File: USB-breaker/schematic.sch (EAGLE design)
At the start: 23 parts, among them K1 G6K-2P, K3 G6K-2P, T1 BC558B, T2 BC548B, X1 PN87520-S, X2 PN87520-S, X3 10104110, X4 UX60SC-MB-5ST

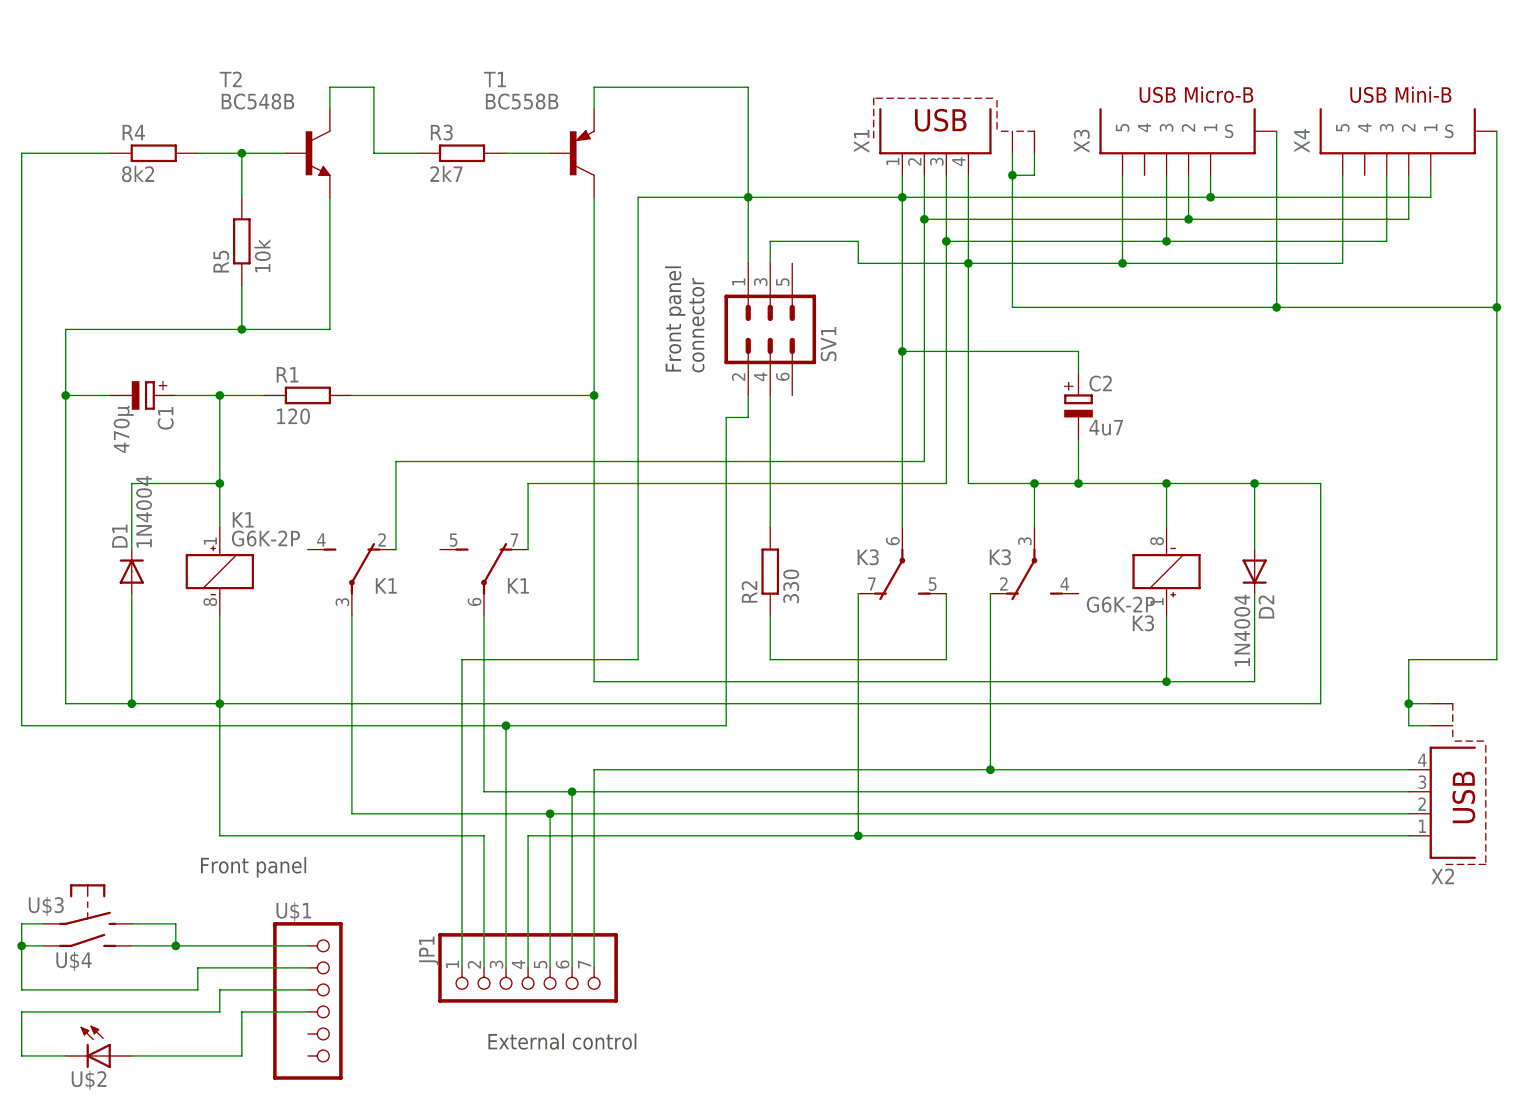
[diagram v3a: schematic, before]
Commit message: Added last details:
- Name / Copyright / License
- OSHW logo
- Processed all warnings in the ERC

Boy, this schematic looks ugly. I'm better using a DIN A4 frame next time...
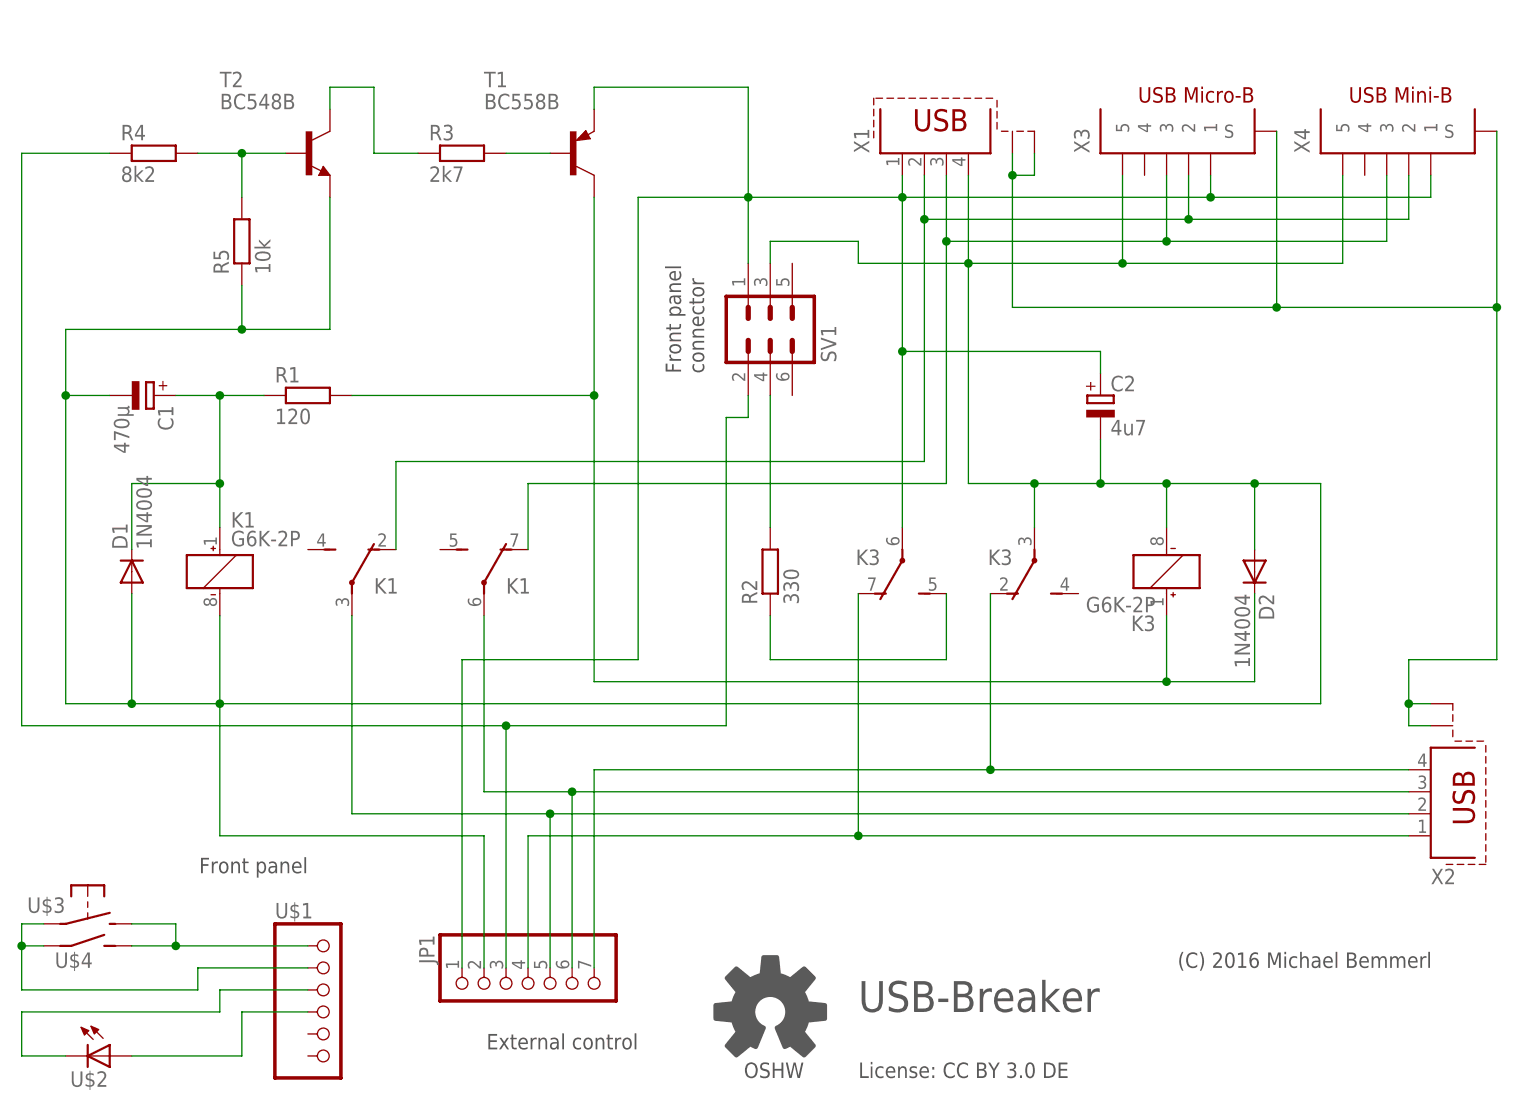
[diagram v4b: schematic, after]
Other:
- note added: "(C) 2016 Michael Bemmerl"
- note added: "License: CC BY 3.0 DE"
- note added: "OSHW"
- note added: "USB-Breaker"
- moved on the sheet: C2
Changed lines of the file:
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@@
 connector</text>
 <text x="78.74" y="12.7" size="1.778" layer="97" rot="R180">External control</text>
+<polygon width="0.508" layer="97">
+<vertex x="95.650653125" y="11.2066875" curve="9.499992"/>
+<vertex x="96.293428125" y="11.537740625"/>
+<vertex x="97.88945" y="10.23613125"/>
+<vertex x="98.98386875" y="11.33055"/>
+<vertex x="97.682259375" y="12.926571875" curve="18.999981"/>
+<vertex x="98.233734375" y="14.257946875"/>
+<vertex x="100.28266875" y="14.466128125"/>
+<vertex x="100.28266875" y="16.013871875"/>
+<vertex x="98.233734375" y="16.222053125" curve="18.999981"/>
+<vertex x="97.682259375" y="17.553428125"/>
+<vertex x="98.98386875" y="19.14945"/>
+<vertex x="97.88945" y="20.24386875"/>
+<vertex x="96.293428125" y="18.942259375" curve="18.999981"/>
+<vertex x="94.962053125" y="19.493734375"/>
+<vertex x="94.753871875" y="21.54266875"/>
+<vertex x="93.206128125" y="21.54266875"/>
+<vertex x="92.997946875" y="19.493734375" curve="18.999981"/>
+<vertex x="91.666571875" y="18.942259375"/>
+<vertex x="90.07055" y="20.24386875"/>
+<vertex x="88.97613125" y="19.14945"/>
+<vertex x="90.277740625" y="17.553428125" curve="18.999981"/>
+<vertex x="89.726265625" y="16.222053125"/>
+<vertex x="87.67733125" y="16.013871875"/>
+<vertex x="87.67733125" y="14.466128125"/>
+<vertex x="89.726265625" y="14.257946875" curve="18.999981"/>
+<vertex x="90.277740625" y="12.926571875"/>
+<vertex x="88.97613125" y="11.33055"/>
+<vertex x="90.07055" y="10.23613125"/>
+<vertex x="91.666571875" y="11.537740625" curve="9.499992"/>
+<vertex x="92.309346875" y="11.2066875"/>
+<vertex x="93.2206125" y="13.406675" curve="-67.500044"/>
+<vertex x="91.995625" y="15.24" curve="-247.500015"/>
+<vertex x="94.7393875" y="13.406675"/>
+</polygon>
+<text x="90.932" y="7.62" size="1.778" layer="97">OSHW</text>
+<text x="140.97" y="20.32" size="1.778" layer="97">(C) 2016 Michael Bemmerl</text>
+<text x="104.14" y="7.62" size="1.778" layer="97">License: CC BY 3.0 DE</text>
+<text x="104.14" y="15.24" size="3.556" layer="97">USB-Breaker</text>
 </plain>
 <instances>
@@
 <instance part="R4" gate="G$1" x="22.86" y="114.3"/>
 <instance part="R5" gate="G$1" x="33.02" y="104.14" rot="R90"/>
-<instance part="C2" gate="G$1" x="129.54" y="86.36"/>
+<instance part="C2" gate="G$1" x="132.08" y="86.36"/>
 </instances>
 <busses>
@@
 <wire x1="58.42" y1="55.88" x2="58.42" y2="20.32" width="0.1524" layer="91"/>
 <pinref part="C2" gate="G$1" pin="+"/>
-<wire x1="129.54" y1="88.9" x2="129.54" y2="91.44" width="0.1524" layer="91"/>
-<wire x1="129.54" y1="91.44" x2="109.22" y2="91.44" width="0.1524" layer="91"/>
+<wire x1="132.08" y1="88.9" x2="132.08" y2="91.44" width="0.1524" layer="91"/>
+<wire x1="132.08" y1="91.44" x2="109.22" y2="91.44" width="0.1524" layer="91"/>
 <junction x="109.22" y="91.44"/>
 </segment>
@@
 <wire x1="116.84" y1="76.2" x2="124.46" y2="76.2" width="0.1524" layer="91"/>
 <wire x1="124.46" y1="76.2" x2="124.46" y2="71.12" width="0.1524" layer="91"/>
-<wire x1="124.46" y1="76.2" x2="129.54" y2="76.2" width="0.1524" layer="91"/>
+<wire x1="124.46" y1="76.2" x2="132.08" y2="76.2" width="0.1524" layer="91"/>
 <junction x="124.46" y="76.2"/>
-<wire x1="129.54" y1="76.2" x2="139.7" y2="76.2" width="0.1524" layer="91"/>
+<wire x1="132.08" y1="76.2" x2="139.7" y2="76.2" width="0.1524" layer="91"/>
 <wire x1="139.7" y1="76.2" x2="139.7" y2="71.12" width="0.1524" layer="91"/>
 <wire x1="139.7" y1="76.2" x2="149.86" y2="76.2" width="0.1524" layer="91"/>
@@
 <junction x="33.02" y="93.98"/>
 <pinref part="C2" gate="G$1" pin="-"/>
-<wire x1="129.54" y1="81.28" x2="129.54" y2="76.2" width="0.1524" layer="91"/>
-<junction x="129.54" y="76.2"/>
+<wire x1="132.08" y1="81.28" x2="132.08" y2="76.2" width="0.1524" layer="91"/>
+<junction x="132.08" y="76.2"/>
 </segment>
 <segment>
@@
 </sheet>
 </sheets>
+<errors>
+</errors>
 </schematic>
 </drawing>

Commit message: Oops, the wrong type of USB connector at X1...
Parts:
- X1: value PN87520-S -> PN61729-S; device con-berg:PN87520-S -> con-berg:PN61729-S
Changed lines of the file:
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@@
 <part name="X4" library="mibe" deviceset="UX60S" device="C-MB-5ST"/>
 <part name="X2" library="con-berg" deviceset="PN87520-S" device=""/>
-<part name="X1" library="con-berg" deviceset="PN87520-S" device=""/>
+<part name="X1" library="con-berg" deviceset="PN61729-S" device=""/>
 <part name="SV1" library="con-harting-ml" deviceset="ML6" device=""/>
 <part name="U$1" library="mibe" deviceset="EXTERNAL_CONNECTOR_6" device=""/>

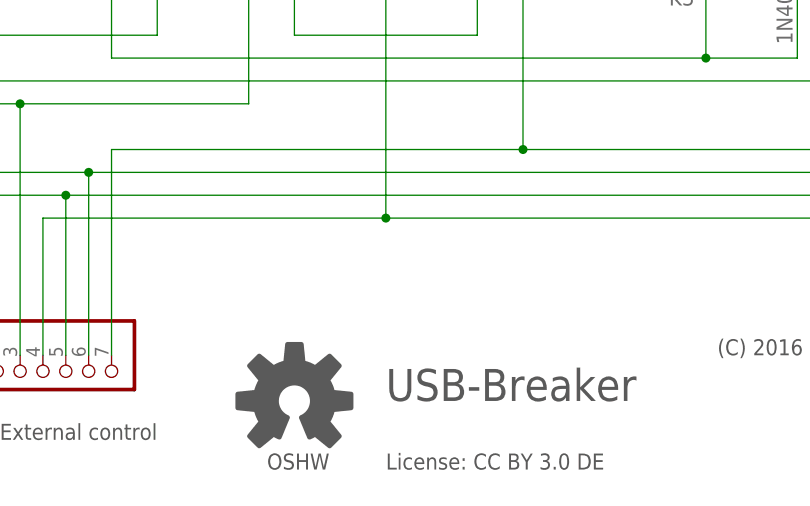
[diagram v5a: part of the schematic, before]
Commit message: Added four mounting holes
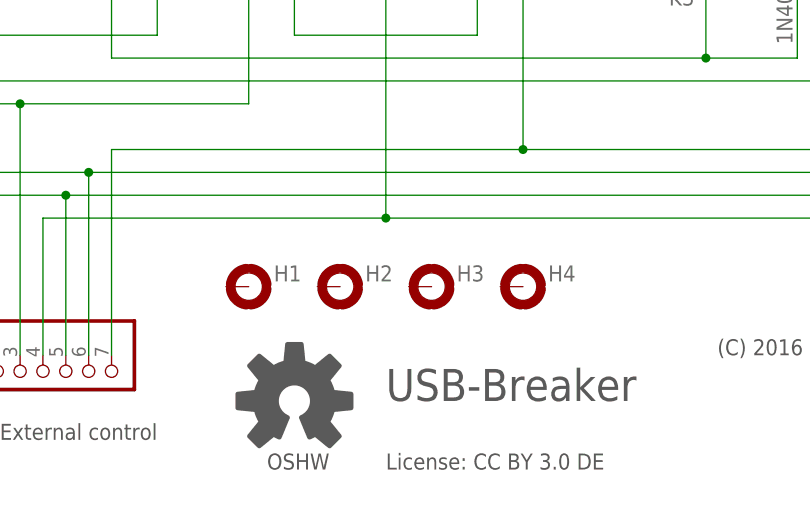
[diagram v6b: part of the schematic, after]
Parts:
- added H1, H2, H3, H4: MOUNT-PAD-ROUND3.0, holes:MOUNT-PAD-ROUND3.0
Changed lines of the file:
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@@
 <part name="R5" library="resistor" deviceset="R-EU_" device="0207/10" value="10k"/>
 <part name="C2" library="resistor" deviceset="CPOL-EU" device="E2.5-6" value="4u7"/>
+<part name="H1" library="holes" deviceset="MOUNT-PAD-ROUND" device="3.0"/>
+<part name="H2" library="holes" deviceset="MOUNT-PAD-ROUND" device="3.0"/>
+<part name="H3" library="holes" deviceset="MOUNT-PAD-ROUND" device="3.0"/>
+<part name="H4" library="holes" deviceset="MOUNT-PAD-ROUND" device="3.0"/>
 </parts>
 <sheets>
@@
 <instance part="R5" gate="G$1" x="33.02" y="104.14" rot="R90"/>
 <instance part="C2" gate="G$1" x="132.08" y="86.36"/>
+<instance part="H1" gate="G$1" x="88.9" y="27.94" smashed="yes">
+<attribute name="NAME" x="91.694" y="28.5242" size="1.778" layer="95"/>
+</instance>
+<instance part="H2" gate="G$1" x="99.06" y="27.94" smashed="yes">
+<attribute name="NAME" x="101.854" y="28.5242" size="1.778" layer="95"/>
+</instance>
+<instance part="H3" gate="G$1" x="109.22" y="27.94" smashed="yes">
+<attribute name="NAME" x="112.014" y="28.5242" size="1.778" layer="95"/>
+</instance>
+<instance part="H4" gate="G$1" x="119.38" y="27.94" smashed="yes">
+<attribute name="NAME" x="122.174" y="28.5242" size="1.778" layer="95"/>
+</instance>
 </instances>
 <busses>

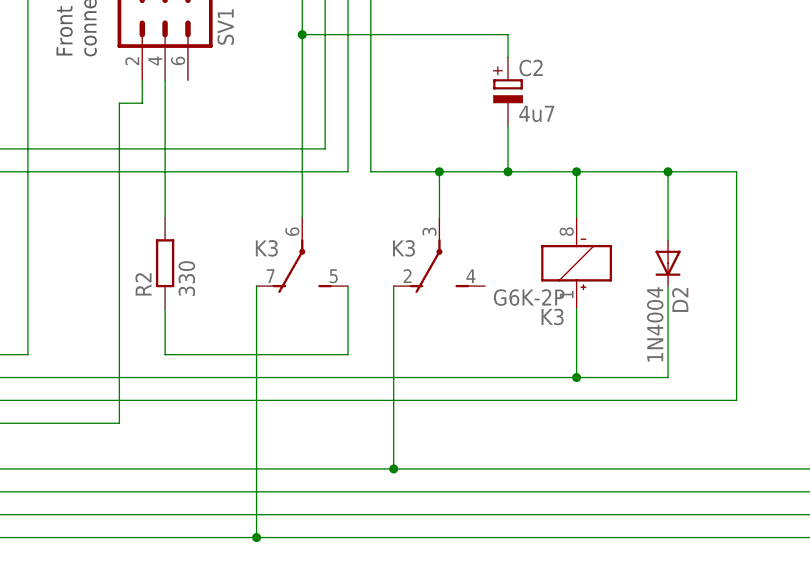
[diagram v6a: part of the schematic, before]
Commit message: The four USB connectors should be properly placed now.
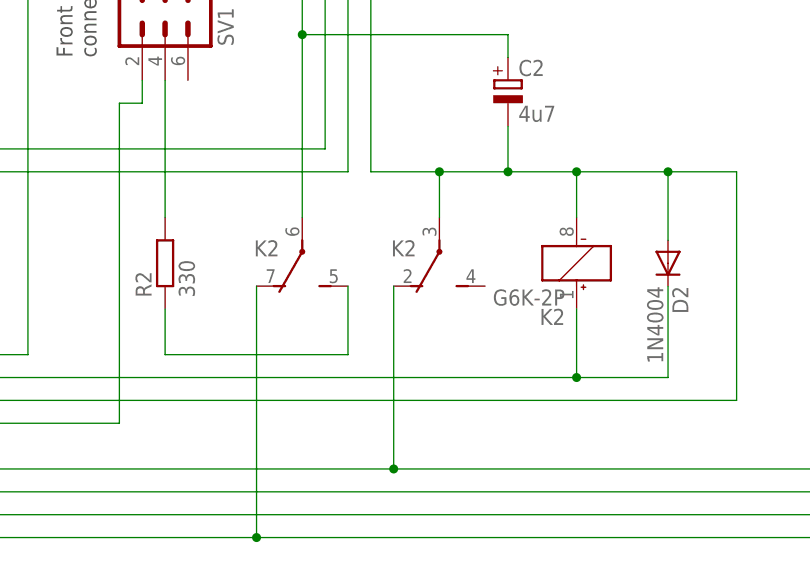
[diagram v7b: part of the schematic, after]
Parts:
- renumbered K3 to K2
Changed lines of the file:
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@@
 <part name="D2" library="diode" deviceset="1N4004" device=""/>
 <part name="K1" library="relay" deviceset="G6K" device="-2P"/>
-<part name="K3" library="relay" deviceset="G6K" device="-2P"/>
+<part name="K2" library="relay" deviceset="G6K" device="-2P"/>
 <part name="X3" library="mibe" deviceset="10104110" device=""/>
 <part name="X4" library="mibe" deviceset="UX60S" device="C-MB-5ST"/>
@@
 <instance part="K1" gate="2" x="45.72" y="63.5"/>
 <instance part="K1" gate="3" x="60.96" y="63.5"/>
-<instance part="K3" gate="1" x="139.7" y="66.04" rot="R180"/>
-<instance part="K3" gate="2" x="124.46" y="68.58" rot="R180"/>
-<instance part="K3" gate="3" x="109.22" y="68.58" rot="R180"/>
+<instance part="K2" gate="1" x="139.7" y="66.04" rot="R180"/>
+<instance part="K2" gate="2" x="124.46" y="68.58" rot="R180"/>
+<instance part="K2" gate="3" x="109.22" y="68.58" rot="R180"/>
 <instance part="X3" gate="G$1" x="144.78" y="121.92" smashed="yes" rot="R90">
 <attribute name="NAME" x="130.81" y="114.3" size="1.778" layer="95" rot="R90"/>
@@
 <wire x1="109.22" y1="109.22" x2="109.22" y2="91.44" width="0.1524" layer="91"/>
 <junction x="109.22" y="109.22"/>
-<pinref part="K3" gate="3" pin="P"/>
+<pinref part="K2" gate="3" pin="P"/>
 <pinref part="X3" gate="G$1" pin="1"/>
 <wire x1="109.22" y1="91.44" x2="109.22" y2="71.12" width="0.1524" layer="91"/>
@@
 <junction x="139.7" y="76.2"/>
 <pinref part="D2" gate="1" pin="A"/>
-<pinref part="K3" gate="1" pin="-"/>
-<pinref part="K3" gate="2" pin="P"/>
+<pinref part="K2" gate="1" pin="-"/>
+<pinref part="K2" gate="2" pin="P"/>
 <pinref part="X3" gate="G$1" pin="5"/>
 <wire x1="116.84" y1="101.6" x2="134.62" y2="101.6" width="0.1524" layer="91"/>
@@
 <wire x1="104.14" y1="35.56" x2="167.64" y2="35.56" width="0.1524" layer="91"/>
 <wire x1="104.14" y1="63.5" x2="104.14" y2="35.56" width="0.1524" layer="91"/>
-<pinref part="K3" gate="3" pin="O"/>
+<pinref part="K2" gate="3" pin="O"/>
 <pinref part="X2" gate="G$1" pin="1"/>
 <pinref part="JP1" gate="A" pin="4"/>
@@
 <wire x1="149.86" y1="53.34" x2="139.7" y2="53.34" width="0.1524" layer="91"/>
 <junction x="139.7" y="53.34"/>
-<pinref part="K3" gate="1" pin="+"/>
+<pinref part="K2" gate="1" pin="+"/>
 <pinref part="T1" gate="G$1" pin="C"/>
 <wire x1="73.66" y1="109.22" x2="73.66" y2="86.36" width="0.1524" layer="91"/>
@@
 <wire x1="93.98" y1="60.96" x2="93.98" y2="55.88" width="0.1524" layer="91"/>
 <wire x1="93.98" y1="55.88" x2="114.3" y2="55.88" width="0.1524" layer="91"/>
-<pinref part="K3" gate="3" pin="S"/>
+<pinref part="K2" gate="3" pin="S"/>
 <wire x1="114.3" y1="55.88" x2="114.3" y2="63.5" width="0.1524" layer="91"/>
 </segment>
@@
 <pinref part="X2" gate="G$1" pin="4"/>
 <wire x1="119.38" y1="43.18" x2="167.64" y2="43.18" width="0.1524" layer="91"/>
-<pinref part="K3" gate="2" pin="O"/>
+<pinref part="K2" gate="2" pin="O"/>
 <wire x1="119.38" y1="63.5" x2="119.38" y2="43.18" width="0.1524" layer="91"/>
 <pinref part="JP1" gate="A" pin="7"/>
